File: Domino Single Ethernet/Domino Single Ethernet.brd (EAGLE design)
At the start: 19.1 x 30.5 mm, 20 parts, among them J1 MH6-1, J2 FR04-2, J3 B50(27-51)FP4-151-A613-B12

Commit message: Changed copyright
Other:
- board text added: "Reference designs are provided "AS IS" and "WITH ALL FAULTS". The Domino Team disclaims all other warranties express or implied, regarding this product, including but not limited to, any implied warranties of merchantibility or fitness for any particular application."
- board text added: "The Domino Team may make changes to specifications and product descriptions at any time, without notice."
- board text added: "© 2014, The Domino Team. All rights reserved."
- board text removed: "Michel Stempin may make changes to specifications and product descriptions at any time, without notice."
- board text removed: "Reference designs are provided "AS IS" and "WITH ALL FAULTS". Michel Stempin disclaims all other warranties express or implied, regarding this product, including but not limited to, any implied warranties of merchantibility or fitness for any particular application."
- board text removed: "© 2014, Michel Stempin. All rights reserved."
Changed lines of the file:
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@@
 See creativecommons.org/licenses/by-sa/4.0/</text>
 <text x="34.29" y="-51.943" size="0.8128" layer="48" ratio="20">Reference designs are provided "AS IS" and "WITH ALL FAULTS".
-Michel Stempin disclaims all other warranties express or implied,
+The Domino Team disclaims all other warranties express or implied,
 regarding this product, including but not limited to, any implied warranties of
 merchantibility or fitness for any particular application.</text>
-<text x="34.29" y="-55.753" size="0.8128" layer="48" ratio="20">Michel Stempin may make changes to specifications and product descriptions
+<text x="34.29" y="-55.753" size="0.8128" layer="48" ratio="20">The Domino Team may make changes to specifications and product descriptions
 at any time, without notice.</text>
-<text x="74.93" y="-41.91" size="1.27" layer="48" ratio="20">© 2014, Michel Stempin.
+<text x="74.93" y="-41.91" size="1.27" layer="48" ratio="20">© 2014, The Domino Team.
 All rights reserved.</text>
 <text x="115.57" y="-57.15" size="1.778" layer="48">Rev.</text>

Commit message: ... and all the files I missed
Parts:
- removed C5, C7: 100n, Domino:C0402
- added C2: 100n, Domino:C0402
- added C3: 2n2, Domino:C1206
- added D1: BLUE, Domino:LED0603
- added D2: WHITE, Domino:LED0603
- added D3, D4, D5, D6: GREEN, Domino:LED0603
- added D7: RED, Domino:LED0603
- added D8: ORANGE, Domino:LED0603
- added D9: YELLOW, Domino:LED0603
- added R1, R2, R3, R4: 49R9, Domino:R0402
- added R10, R11, R9: 270R, Domino:R0603
- added R12: 150R, Domino:R0603
- added R13, R14: 330R, Domino:R0603
- added U$13: (no value), Domino:DOMINO_LOGO_SMALL
- added U$14: (no value), Domino:CE_LOGO_SMALL
- added U$15: (no value), Domino:FCC_LOGO_SMALL
- added U$16: (no value), Domino:OPEN_HARDWARE_LOGO
- added U$17: (no value), Domino:RECYCLE_BIN_LOGO
- added U$18: (no value), Domino:ROHS_LOGO
- C1: value 2n2 -> 100n; device Domino:C1206 -> Domino:C0402
- J1: value MH6-1 -> MH18-1; device Domino:MH6-1-0.1 -> Domino:MH18-1-0.1
- J2: value FR04-2 -> MH18-1; device Domino:FR04-2-0.1 -> Domino:MH18-1-0.1
- R5: value 49R9 -> 330R; device Domino:R0402 -> Domino:R0603
- R6, R7, R8: value 49R9 -> 270R; device Domino:R0402 -> Domino:R0603
- moved U$5 28.1 mm to (44.5, 10.8)
- moved U$6 27.4 mm to (36.2, 10.8)
- moved J2 27.3 mm to (1.27, 1.27), flipped to the bottom, turned to 180 degrees
- moved U$9 25.7 mm to (43.2, 19.1)
- moved U$8 23.7 mm to (42.5, 3.17)
- moved R8 22.8 mm to (26.7, 28.7), turned to 270 degrees
- moved R7 22.3 mm to (24.1, 28.7), turned to 270 degrees
- moved C1 19.1 mm to (20.3, 15.2), flipped to the top, turned to 180 degrees
- moved U$4 18.3 mm to (24.1, 19.7), flipped to the bottom, turned to 270 degrees
- moved U$7 17.3 mm to (25.4, 12.7)
- moved R5 12.1 mm to (18.4, 30.0)
- moved R6 11.9 mm to (21.6, 28.7), flipped to the bottom, turned to 270 degrees
- moved J3 9.09 mm to (7.62, 16.5), turned to 270 degrees
- moved C4 8.11 mm to (17.3, 26.9)
- moved J1 2.54 mm to (1.27, 31.8)
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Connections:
- removed net P4_LED_L_A: J2.6, J3.13
- removed net P4_LED_L_C: J2.8, J3.14
- removed net P4_LED_R_A: J2.2, J3.11
- removed net P4_LED_R_C: J2.4, J3.12
- removed net VC12: J2.5, J3.9
- removed net VC36: J2.7, J3.10
- removed net VC45: J2.1, J3.4
- removed net VC78: J2.3, J3.5
- new net +3V3: D7.2, D8.2, D9.2, J1.8, J3.13, R5.2
- new net GREEN_LED: J3.11, R5.1
- new net LAN1_LED: D3.2, R8.2
- new net LAN2_LED: D4.2, R9.2
- new net LAN3_LED: D5.2, R10.2
- new net LAN4_LED: D6.2, R11.2
- new net LED0: J1.9, R6.1
- new net LED1: J1.10, R7.1
- new net LED2: J1.11, R8.1
- new net LED3: J1.12, R9.1
- new net LED4: J1.13, R10.1
- new net LED5: J1.14, R11.1
- new net LED6: J1.15, R12.1
- new net LED7: J1.16, R13.1
- new net LED8: J1.17, R14.1
- new net SYS_LED: D8.1, R13.2
- new net USB_LED: D2.2, R7.2
- new net WAN_LED: D7.1, J3.14, R12.2
- new net WLAN_LED: D1.2, R6.2
- new net WPS_LED: D9.1, R14.2
- net +2VA_ETH_OUT: now also C4.2, J2.14; no longer C7.2, J1.6
- net GND: now also C2.1, C3.1, D1.1, D2.1, D3.1, D4.1, D5.1, D6.1, J1.18, J2.9, J3.12; no longer C5.1, C7.1, J1.1
- net P4_RX: now also C1.2, R1.1, R2.1; no longer C4.2, R5.1, R6.1
- net P4_RX_N: now also J2.11, R2.2; no longer J1.3, R6.2
- net P4_RX_P: now also J2.10, R1.2; no longer J1.2, R5.2
- net P4_TX: now also C2.2, R3.1, R4.1; no longer C5.2, R7.1, R8.1
- net P4_TX_N: now also J2.13, R4.2; no longer J1.5, R8.2
- net P4_TX_P: now also J2.12, R3.2; no longer J1.4, R7.2
- net SHIELD: now also C3.2; no longer C1.2
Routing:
- net +3V3: track 0.00 -> 57.8 mm
- net WAN_LED: track 0.00 -> 51.8 mm, vias 0 -> 1
- net P4_LED_R_A: track 34.8 -> 0.00 mm
- net +2VA_ETH_OUT: track 17.1 -> 50.2 mm
- net P4_LED_R_C: track 31.0 -> 0.00 mm
- net P4_LED_L_A: track 27.7 -> 0.00 mm
- net P4_LED_L_C: track 27.3 -> 0.00 mm
- net VC45: track 19.3 -> 0.00 mm
- net GND: track 0.00 -> 18.6 mm, vias 16 -> 108
- net GREEN_LED: track 0.00 -> 17.9 mm
- net P4_TX_N: track 19.0 -> 35.1 mm
- net VC78: track 15.0 -> 0.00 mm
- net P4_TX_P: track 16.4 -> 30.9 mm
- net VC36: track 11.4 -> 0.00 mm
- net VC12: track 9.69 -> 0.00 mm
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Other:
- board size 19.1 x 30.5 mm -> 45.7 x 33 mm
- board text added: "+3V3"
- board text added: "ELD2"
- board text added: "LAN1"
- board text added: "LAN2"
- board text added: "LAN3"
- board text added: "LAN4"
- board text added: "LED0"
- board text added: "LED1"
- board text added: "LED3"
- board text added: "LED4"
- board text added: "LED5"
- board text added: "LED6"
- board text added: "LED7"
- board text added: "LED8"
- board text added: "SYS"
- board text added: "USB"
- board text added: "WLAN"
- board text added: "WPS"
- board text removed: "LED"
- board text removed: "PoE"
- board text removed: "Rev. A"

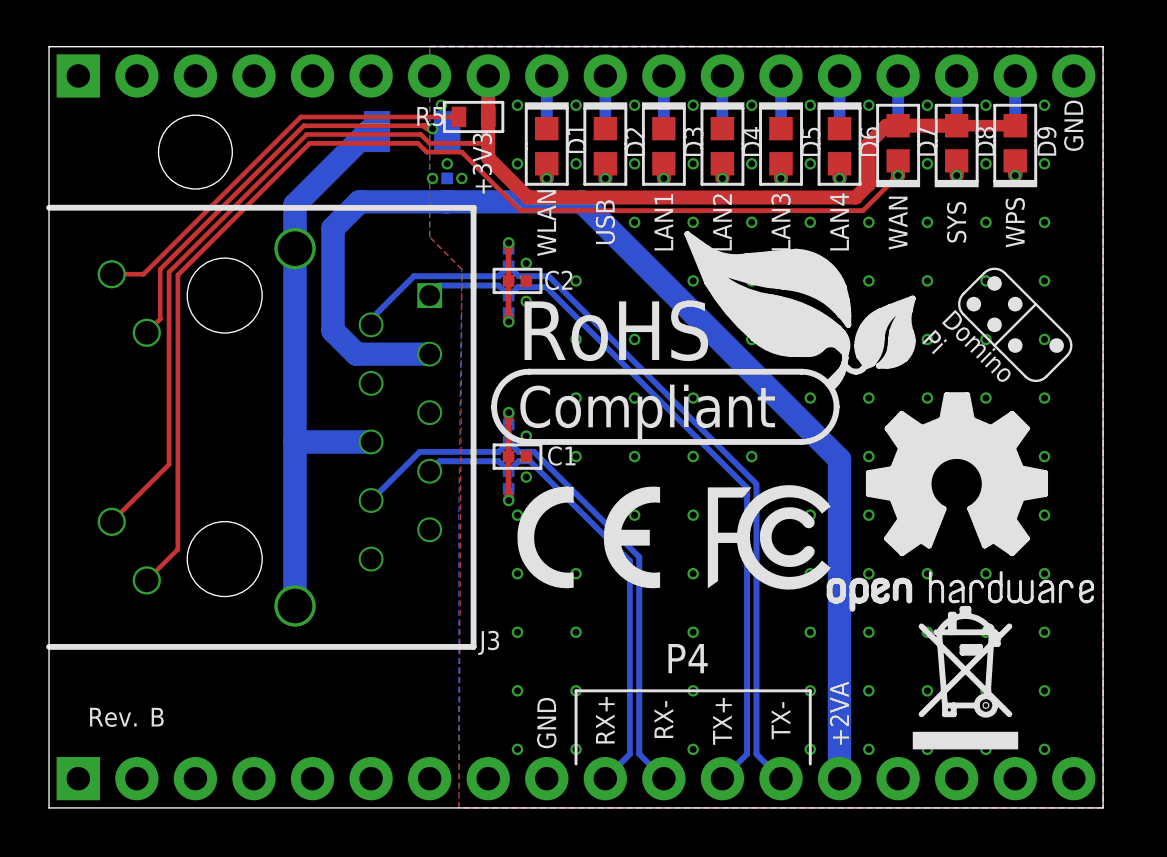
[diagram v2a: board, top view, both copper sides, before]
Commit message: Made Single Ethernet tile with component on top side only
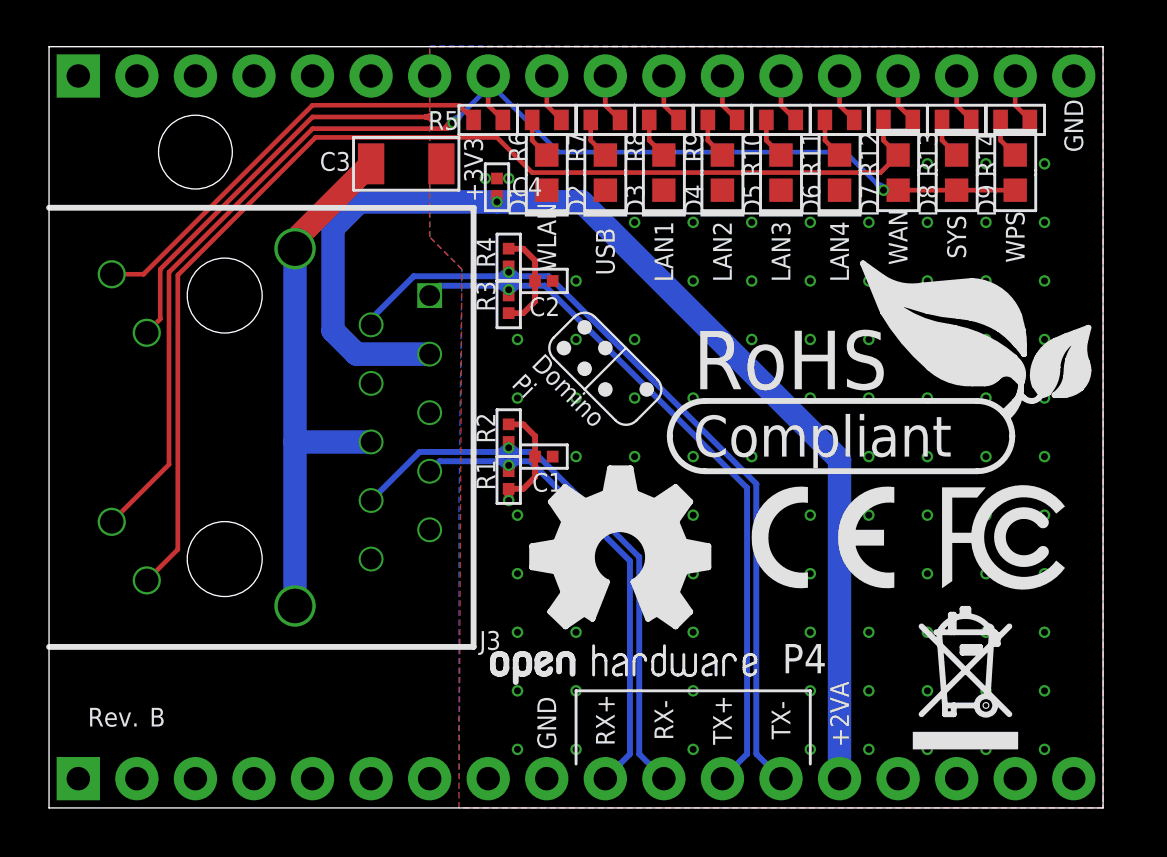
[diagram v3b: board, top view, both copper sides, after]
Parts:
- moved U$13 17.9 mm to (24.1, 19.1)
- moved U$16 14.9 mm to (24.8, 10.8)
- moved U$14 10.2 mm to (30.5, 9.53)
- moved U$15 10.2 mm to (38.7, 9.53)
- moved U$18 7.73 mm to (27.9, 15.2)
- moved C4 2.16 mm to (19.4, 26.9), flipped to the top
- moved C3 1.42 mm to (15.5, 27.9), flipped to the top, turned to 180 degrees
- moved D7 1.27 mm to (36.8, 27.6), turned to 270 degrees
- moved D8 1.27 mm to (39.4, 27.6), turned to 270 degrees
- moved D9 1.27 mm to (41.9, 27.6), turned to 270 degrees
- moved C1 1.14 mm to (21.5, 15.2)
- moved C2 1.14 mm to (21.5, 22.9)
- moved D1 1.14 mm to (21.6, 27.6), turned to 90 degrees
- moved D2 1.14 mm to (24.1, 27.6), turned to 90 degrees
- moved D3 1.14 mm to (26.7, 27.6), turned to 90 degrees
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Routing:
- net +3V3: track 57.8 -> 61.0 mm, vias 0 -> 2
- net P4_RX: track 9.27 -> 6.10 mm, vias 2 -> 1
- net P4_TX_P: track 30.9 -> 33.3 mm, vias 0 -> 1
- net P4_RX_P: track 20.9 -> 23.2 mm, vias 0 -> 1
- net P4_TX_N: track 35.1 -> 37.3 mm, vias 0 -> 1
- net P4_RX_N: track 24.8 -> 27.1 mm, vias 0 -> 1
- net P4_TX: track 6.29 -> 4.48 mm, vias 2 -> 0
- net SHIELD: track 25.6 -> 23.8 mm
- net WAN_LED: track 51.8 -> 50.3 mm, vias 1 -> 0
- net GREEN_LED: track 17.9 -> 19.0 mm
- net WLAN_LED: track 1.40 -> 1.79 mm, vias 1 -> 0
- net LAN3_LED: track 1.40 -> 1.79 mm, vias 1 -> 0
- net LAN2_LED: track 1.40 -> 1.79 mm, vias 1 -> 0
- net LAN1_LED: track 1.40 -> 1.79 mm, vias 1 -> 0
- net WPS_LED: track 1.40 -> 1.79 mm, vias 1 -> 0
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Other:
- board text added: "LED2"

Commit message: Domino Single Ethernet tile Revision B
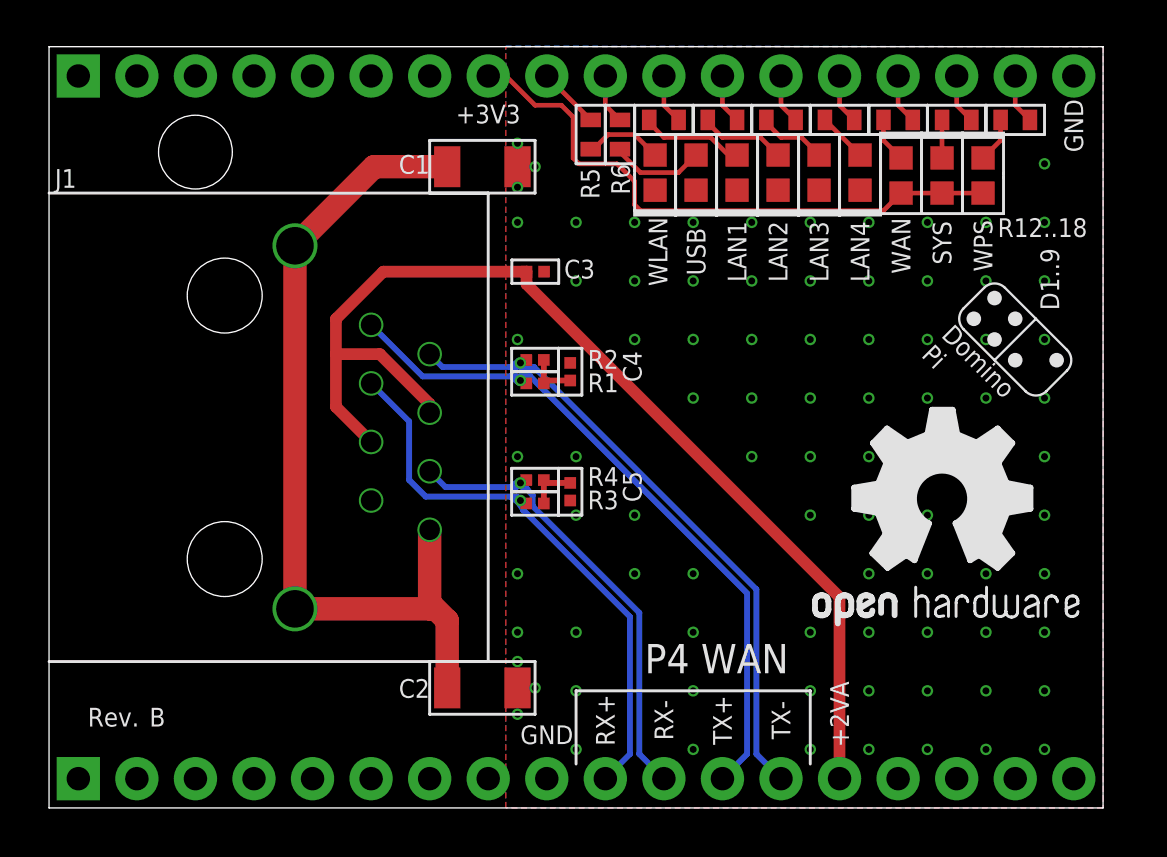
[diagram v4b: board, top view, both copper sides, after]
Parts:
- removed R14: 330R, Domino:R0603
- removed U$14: (no value), Domino:CE_LOGO_SMALL
- removed U$15: (no value), Domino:FCC_LOGO_SMALL
- removed U$17: (no value), Domino:RECYCLE_BIN_LOGO
- removed U$18: (no value), Domino:ROHS_LOGO
- added C5: 100n, Domino:C0402
- C1, C2: value 100n -> 2n2; device Domino:C0402 -> Domino:C1206
- C3: value 2n2 -> 100n; device Domino:C1206 -> Domino:C0402
- J1: value MH18-1 -> 11A009-1702-00; device Domino:MH18-1-0.1 -> Domino:11A009-1702-00
- J3: value B50(27-51)FP4-151-A613-B12 -> MH18-1; device Domino:B50(27-51)FP4-151-A613-B12 -> Domino:MH18-1-0.1
- R11: value 270R -> 330R
- R12: value 150R -> 330R
- R5: value 330R -> 270R
- moved U$8 38.2 mm to (5.71, 13.3)
- moved J2 30.5 mm to (1.27, 31.8)
- moved U$5 27.7 mm to (17.8, 3.17)
- moved U$6 27.7 mm to (9.53, 3.17)
- moved C2 17.9 mm to (18.8, 5.21)
- moved U$13 17.8 mm to (41.9, 20.3)
- moved J3 16.5 mm to (1.27, 1.27), flipped to the bottom, turned to 180 degrees
- moved J1 16.5 mm to (7.62, 16.5), flipped to the top, turned to 270 degrees
- moved U$4 16.1 mm to (39.4, 14.6)
- moved U$16 14.2 mm to (38.7, 13.3)
- moved C1 12.9 mm to (18.8, 27.8)
- moved R4 9.72 mm to (21.1, 14.2), turned to 180 degrees
- moved R3 8.71 mm to (21.1, 13.2), turned to 180 degrees
- moved C4 8.61 mm to (22.6, 18.9)
- moved C3 7.29 mm to (21.1, 23.3)
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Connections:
- removed net GREEN_LED: J3.11, R5.1
- net +2VA_ETH_OUT: now also C3.2, J1.4, J1.5, J3.14; no longer C4.2, J2.14, J3.3
- net +3V3: now also J2.8; no longer J1.8, J3.13, R5.2
- net GND: now also C5.1, J2.18, J3.9; no longer J1.18, J2.9, J3.12
- net LAN1_LED: now also R7.2; no longer R8.2
- net LAN2_LED: now also R8.2; no longer R9.2
- net LAN3_LED: now also R9.2; no longer R10.2
- net LAN4_LED: now also R10.2; no longer R11.2
- net LED0: now also J2.9, R5.1; no longer J1.9, R6.1
- net LED1: now also J2.10, R6.1; no longer J1.10, R7.1
- net LED2: now also J2.11, R7.1; no longer J1.11, R8.1
- net LED3: now also J2.12, R8.1; no longer J1.12, R9.1
- net LED4: now also J2.13, R9.1; no longer J1.13, R10.1
- net LED5: now also J2.14, R10.1; no longer J1.14, R11.1
- net LED6: now also J2.15, R11.1; no longer J1.15, R12.1
- net LED7: now also J2.16, R12.1; no longer J1.16, R13.1
- net LED8: now also J2.17, R13.1; no longer J1.17, R14.1
- net P4_RX: now also C5.2, R3.1, R4.1; no longer C1.2, R1.1, R2.1
- net P4_RX_N: now also J1.6, J3.11, R4.2; no longer J2.11, J3.8, R2.2
- net P4_RX_P: now also J1.3, J3.10, R3.2; no longer J2.10, J3.7, R1.2
- net P4_TX: now also C4.2, R1.1, R2.1; no longer C2.2, R3.1, R4.1
- net P4_TX_N: now also J1.2, J3.13, R2.2; no longer J2.13, J3.2, R4.2
- net P4_TX_P: now also J1.1, J3.12, R1.2; no longer J2.12, J3.1, R3.2
- net SHIELD: now also C1.2, C2.2, J1.8, J1.SH$1, J1.SH$2; no longer C3.2, J3.6, J3.SH$1, J3.SH$2
- net SYS_LED: now also R12.2; no longer R13.2
- net USB_LED: now also R6.2; no longer R7.2
- net WAN_LED: now also R11.2; no longer J3.14, R12.2
- net WLAN_LED: now also R5.2; no longer R6.2
- net WPS_LED: now also R13.2; no longer R14.2
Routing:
- net WAN_LED: track 50.3 -> 1.97 mm
- net +3V3: track 61.0 -> 25.8 mm, vias 2 -> 0
- net GREEN_LED: track 19.0 -> 0.00 mm
- net GND: track 18.8 -> 0.00 mm, vias 88 -> 86
- net SHIELD: track 23.8 -> 37.0 mm
- net P4_TX_N: track 37.3 -> 29.8 mm
- net P4_RX_N: track 27.1 -> 22.2 mm
- net P4_RX: track 6.10 -> 2.21 mm, vias 1 -> 0
- net P4_RX_P: track 23.2 -> 27.1 mm
- net LAN1_LED: track 1.79 -> 4.52 mm
- net USB_LED: track 1.79 -> 4.11 mm
- net P4_TX: track 4.48 -> 2.21 mm
- net +2VA_ETH_OUT: track 50.2 -> 48.0 mm, vias 1 -> 0
- net LAN2_LED: track 1.79 -> 3.75 mm
- net WLAN_LED: track 1.79 -> 3.43 mm
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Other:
- board text added: "D1..9"
- board text added: "P4 WAN"
- board text added: "R12..18"
- board text removed: "P4"

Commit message: Domino Single Ethernet Rev. C: changed Logos
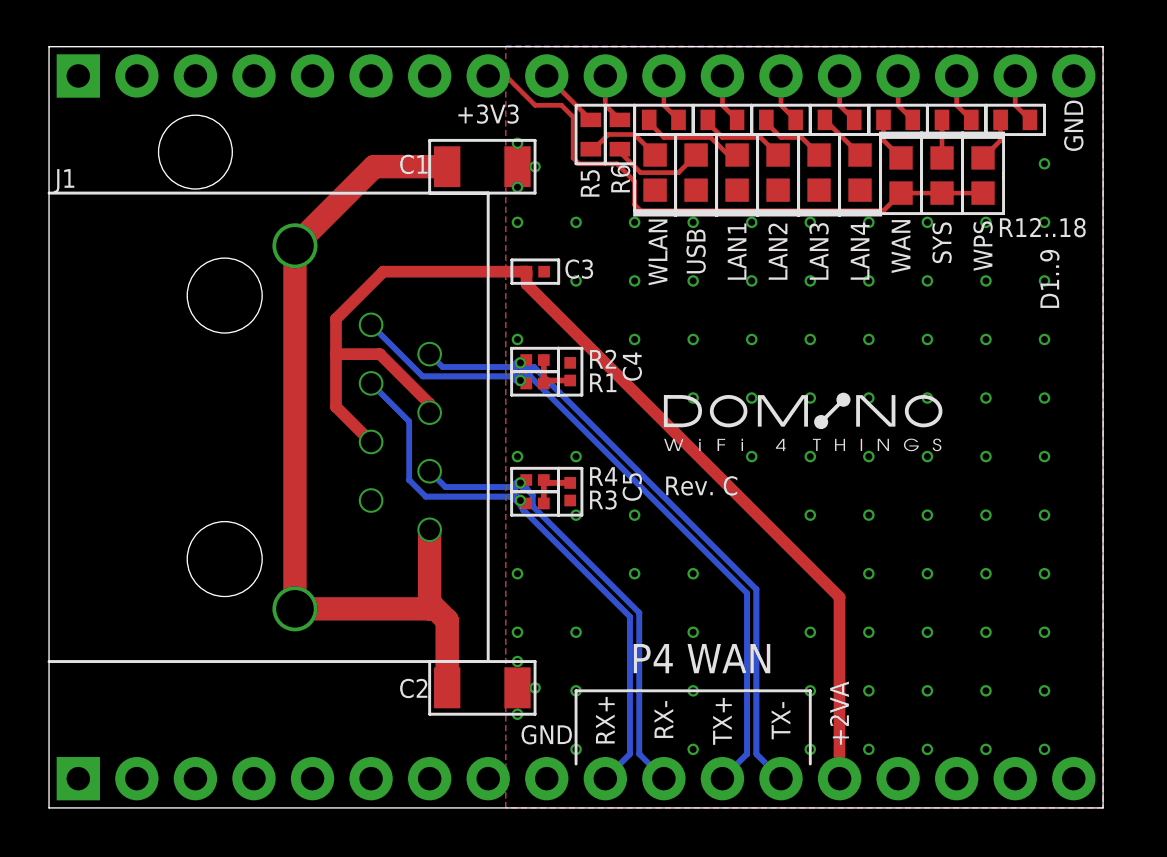
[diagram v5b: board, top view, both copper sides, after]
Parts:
- removed U$16: (no value), Domino:OPEN_HARDWARE_LOGO
- added U$10: DOMINO_LOGO, Domino:DOMINO_LOGO
- added U$11: (no value), Domino:DOMINO_LOGO_SMALL
- U$13: device Domino:DOMINO_LOGO_SMALL -> Domino:ESD_LOGO
- moved U$8 19.1 mm to (24.8, 14.6)
- moved U$13 14.4 mm to (31.8, 10.2), flipped to the bottom, turned to 0 degrees
- moved U$4 12.8 mm to (26.7, 16.5), flipped to the top, turned to 0 degrees
- moved U$7 7.62 mm to (38.1, 13.3)
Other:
- board text removed: "Domino Core"
- board text removed: "Domino Pi"
- board text removed: "Domino Qi"

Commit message: Domnio Single Ethernet Rev. D: changed silkscreen font ratio to 20%
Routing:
- net P4_RX_P: track 27.1 -> 26.0 mm
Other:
- board text added: "© 2014-2015, The Domino Team. All rights reserved."
- board text removed: "© 2014, The Domino Team. All rights reserved."
